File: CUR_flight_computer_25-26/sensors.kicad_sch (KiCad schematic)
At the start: 13 parts, among them U2 IIS2MDC, U3 LPS22HB, U4 LSM6DSV80X

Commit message: Update sensors.kicad_sch
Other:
- note added: "reccomends "aluminum" capacitor here"
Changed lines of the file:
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@@
 	(generator_version "9.0")
 	(paper "A4")
+	(text "reccomends \"aluminum\" capacitor here"
+		(exclude_from_sim no)
+		(at 103.632 119.634 0)
+		(effects
+			(font
+				(size 1.27 1.27)
+			)
+		)
+	)
 	(junction
 		(at 72.39 113.03)

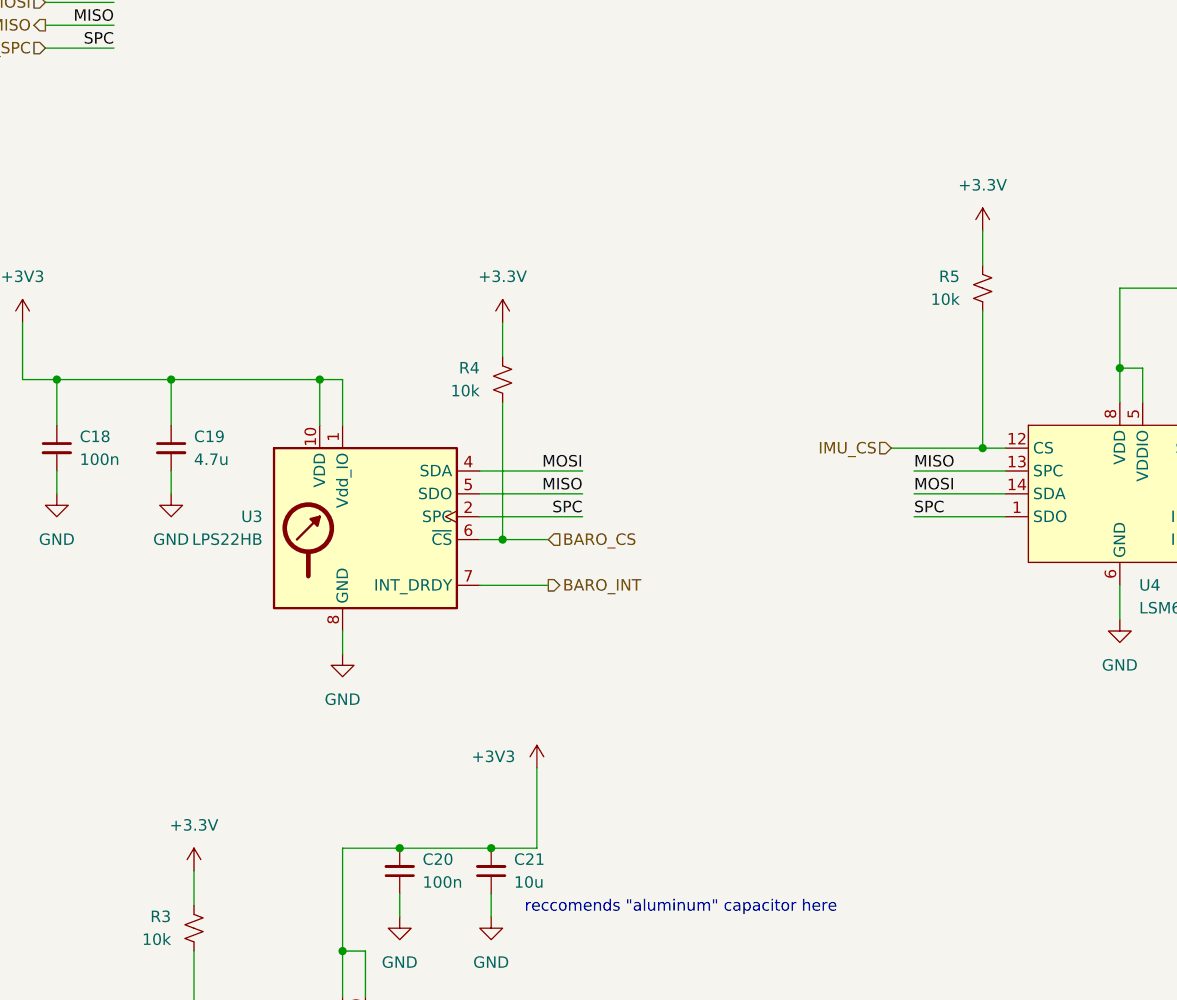
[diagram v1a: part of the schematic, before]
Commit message: most of layout figured out
trouble finding room for power
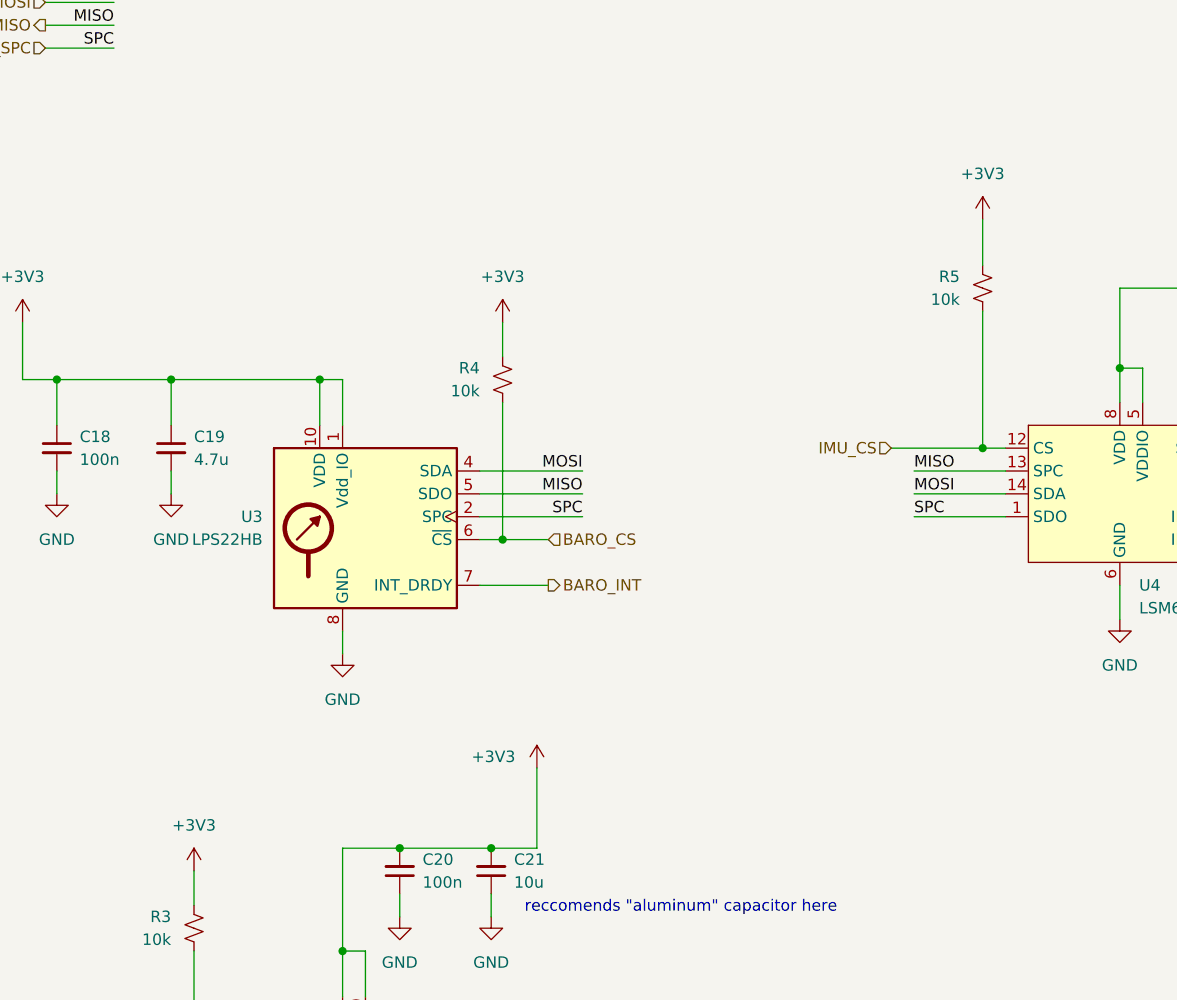
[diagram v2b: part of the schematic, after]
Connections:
- net +3.3V is gone; now on net +3V3: R3.1, R4.1, R5.1

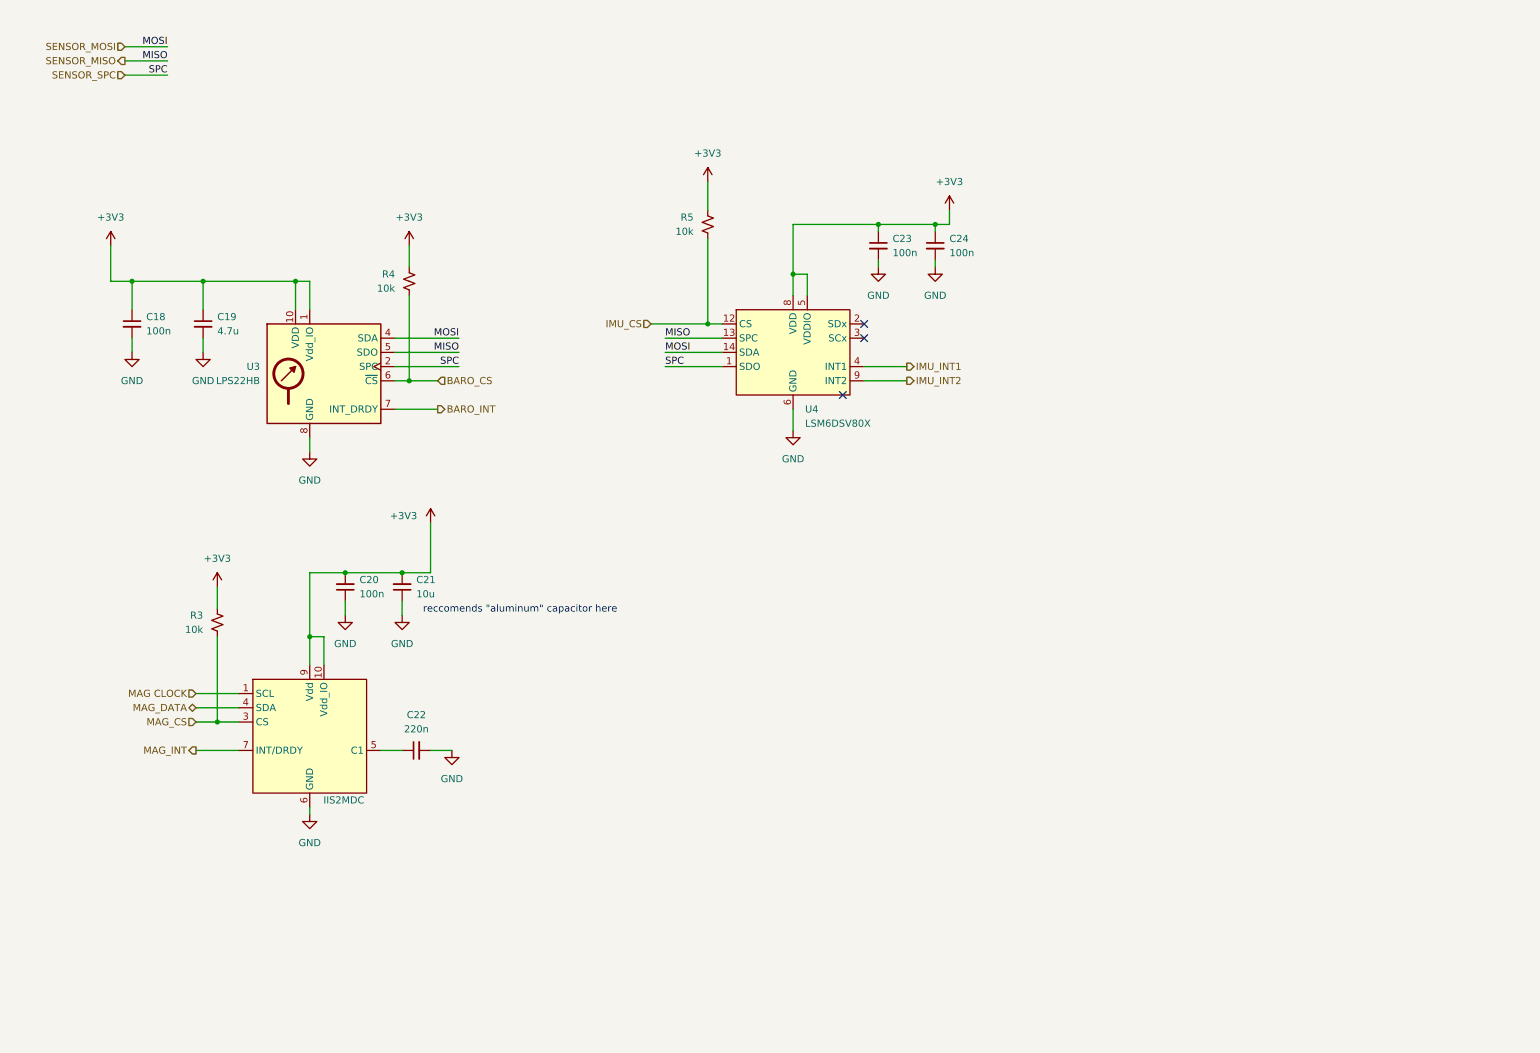
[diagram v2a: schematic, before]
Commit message: added testpoints to schematic
need to update layout
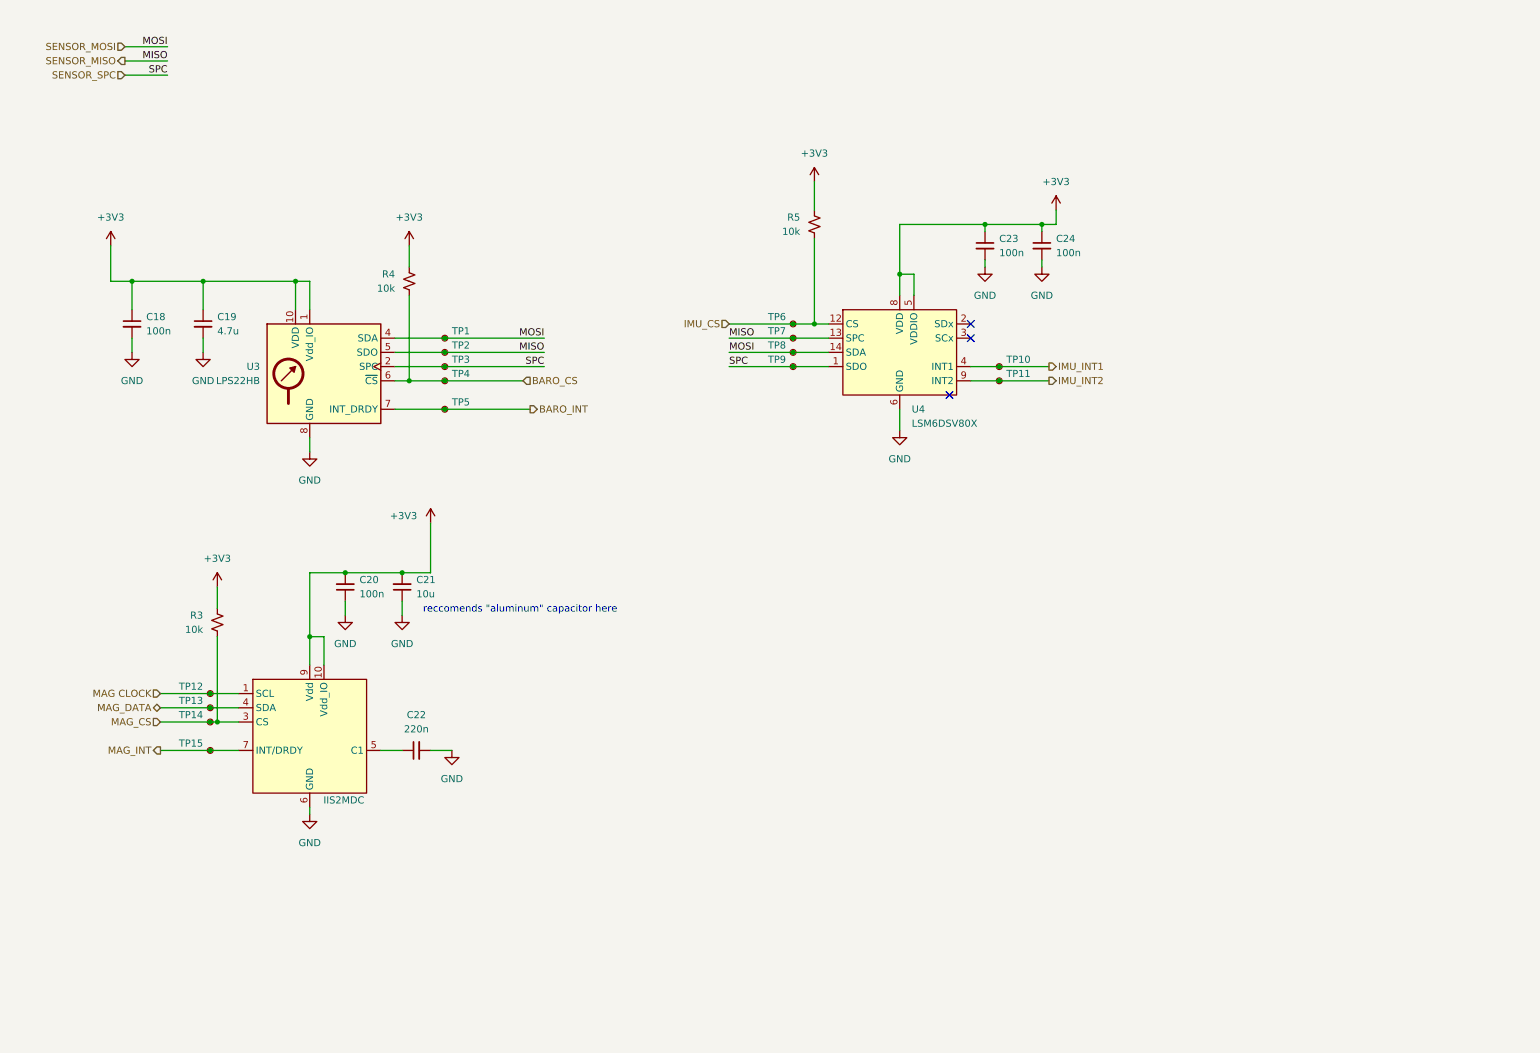
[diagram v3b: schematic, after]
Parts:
- added TP1, TP10, TP11, TP12, TP13, TP14, TP15, TP2, TP3, TP4, TP5, TP6, TP7, TP8, TP9: TestPoint_Small, TestPoint_KOASpeer:TestPoint_Chip_RCUCTE_0603, symbol Connector:TestPoint_Small
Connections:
- net BARO_CS: now also TP4.1
- net BARO_INT: now also TP5.1
- net IMU_CS: now also TP6.1
- net IMU_INT1: now also TP10.1
- net IMU_INT2: now also TP11.1
- net MAG CLOCK: now also TP12.1
- net MAG_CS: now also TP14.1
- net MAG_DATA: now also TP13.1
- net MAG_INT: now also TP15.1
- net SENSOR_MISO: now also TP2.1, TP7.1
- net SENSOR_MOSI: now also TP1.1, TP8.1
- net SENSOR_SPC: now also TP3.1, TP9.1
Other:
- moved on the sheet: C23, C24, R5, U4

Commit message: Update sensors.kicad_sch
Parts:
- removed TP7, TP8, TP9: TestPoint_Small, TestPoint_KOASpeer:TestPoint_Chip_RCUCTE_0603, symbol Connector:TestPoint_Small

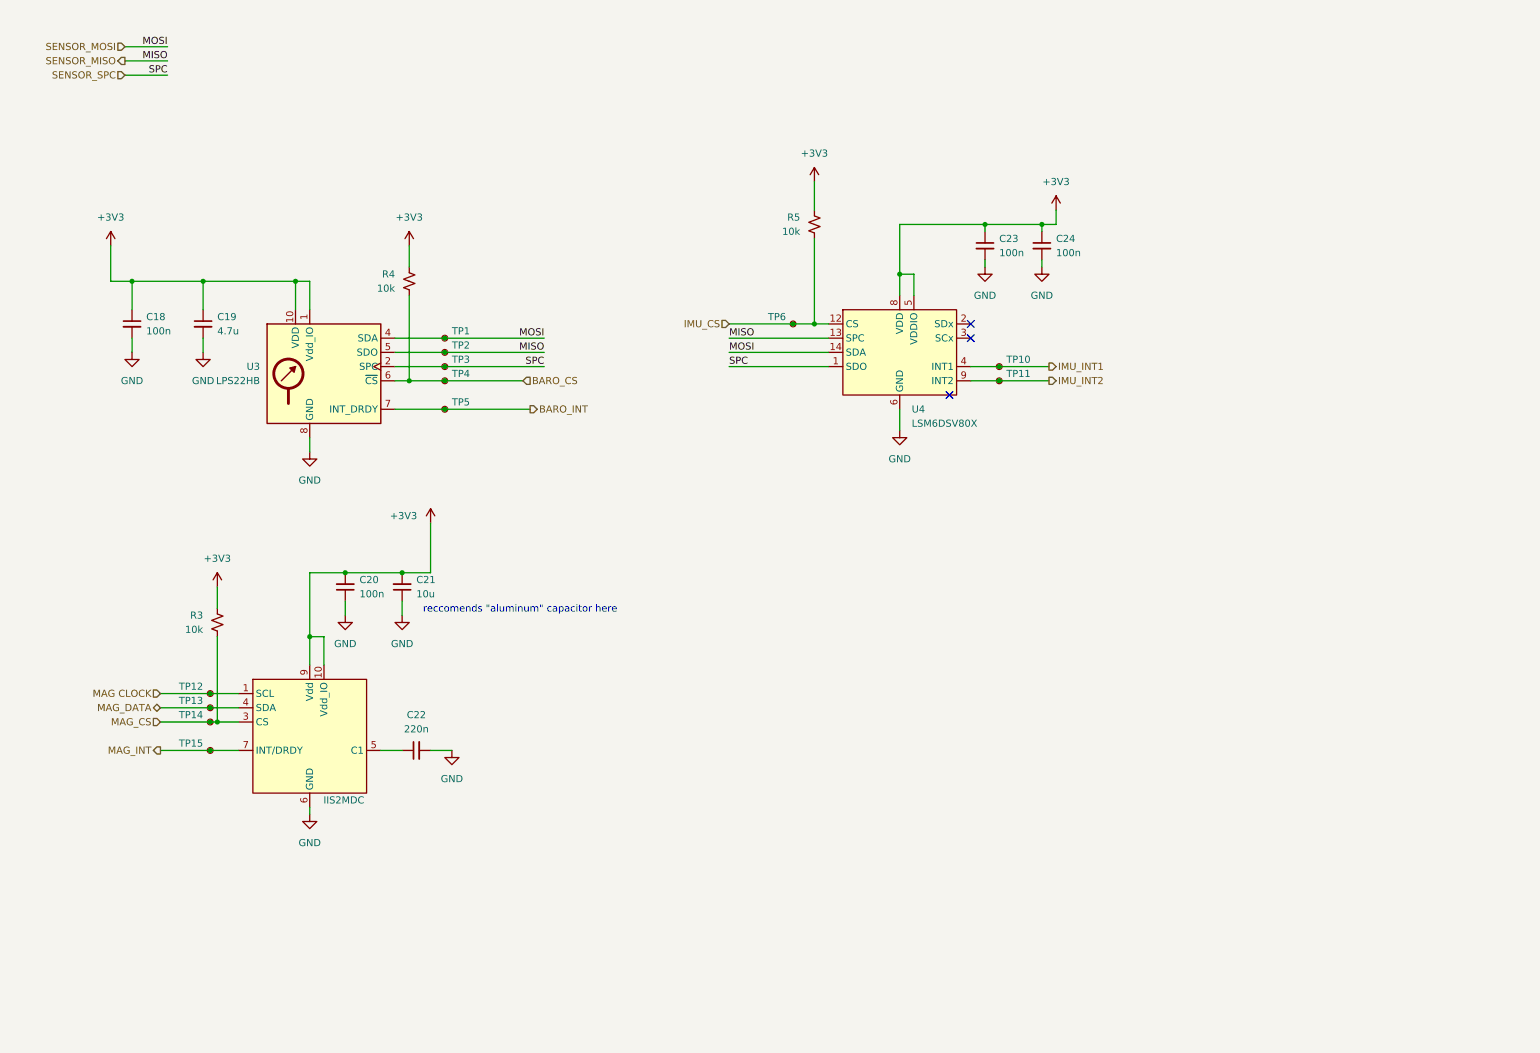
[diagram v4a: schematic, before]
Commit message: Apply MPNs for capacitors and connectors
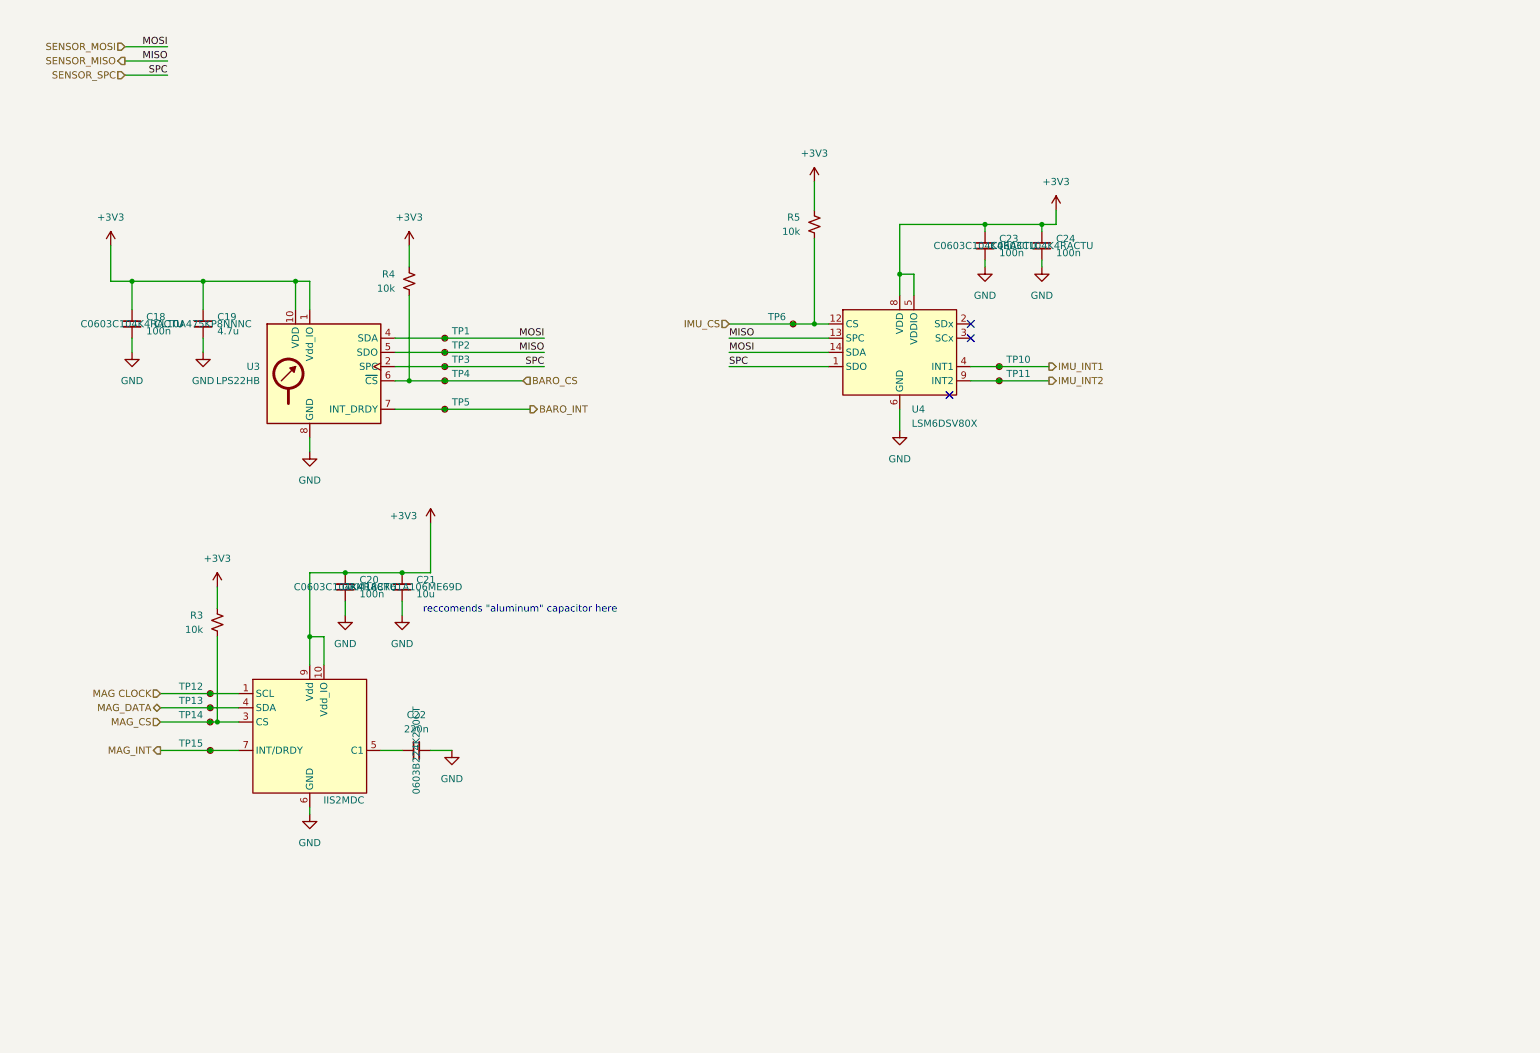
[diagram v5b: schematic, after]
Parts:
- C18, C20, C23, C24: MPN (none) -> C0603C104K4RACTU
- C19: MPN (none) -> CL10A475KP8NNNC
- C21: MPN (none) -> GRM188R61A106ME69D
- C22: MPN (none) -> 0603B224K250CT
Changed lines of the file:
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@@
+			)
+		)
+		(property "MPN" "C0603C104K4RACTU"
+			(at 34.29 68.58 0)
+			(effects
+				(font
+					(size 1.27 1.27)
+				)
 			)
 		)
@@
 				)
 				(hide yes)
+			)
+		)
+		(property "MPN" "0603B224K250CT"
+			(at 85.09 144.78 0)
+			(effects
+				(font
+					(size 1.27 1.27)
+				)
 			)
 		)
@@
 			)
 		)
+		(property "MPN" "CL10A475KP8NNNC"
+			(at 46.99 68.58 0)
+			(effects
+				(font
+					(size 1.27 1.27)
+				)
+			)
+		)
 		(pin "2"
 		)
@@
 			)
 		)
+		(property "MPN" "C0603C104K4RACTU"
+			(at 196.85 54.61 0)
+			(effects
+				(font
+					(size 1.27 1.27)
+				)
+			)
+		)
 		(pin "1"
 		)
@@
 				)
 				(hide yes)
+			)
+		)
+		(property "MPN" "C0603C104K4RACTU"
+			(at 186.69 54.61 0)
+			(effects
+				(font
+					(size 1.27 1.27)
+				)
 			)
 		)
@@
 			)
 		)
+		(property "MPN" "GRM188R61A106ME69D"
+			(at 82.55 115.57 0)
+			(effects
+				(font
+					(size 1.27 1.27)
+				)
+			)
+		)
 		(pin "2"
 		)
@@
 			)
 		)
+		(property "MPN" "C0603C104K4RACTU"
+			(at 72.39 115.57 0)
+			(effects
+				(font
+					(size 1.27 1.27)
+				)
+			)
+		)
